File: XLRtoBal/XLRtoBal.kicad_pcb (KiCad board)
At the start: 2 copper layers, 85 x 93 mm, 55 parts, among them J1 XLR3, J10 Conn_Coaxial, J11 Conn_Coaxial, J2 Conn_01x04, J3 Conn_01x04, J4 XLR3, J5 Conn_01x04, J6 Conn_01x01, J7 Conn_01x01, J8 Conn_01x01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

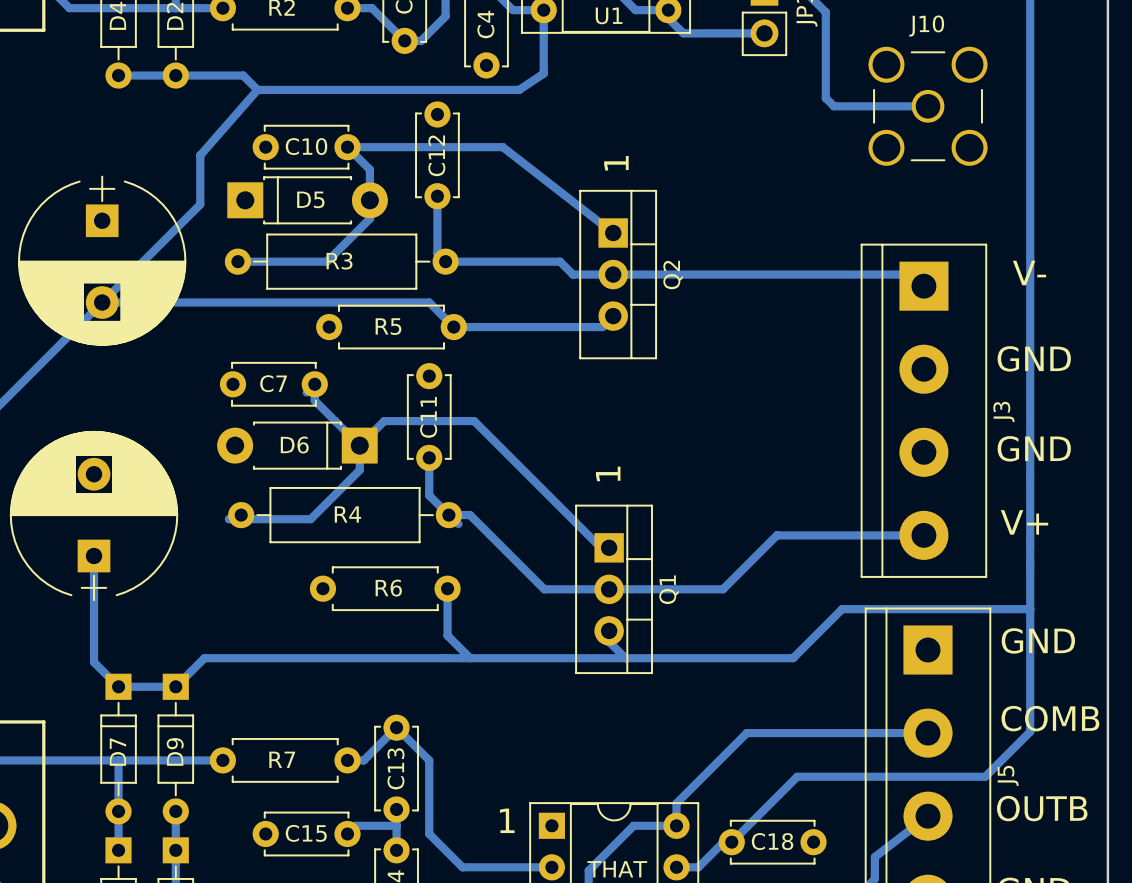
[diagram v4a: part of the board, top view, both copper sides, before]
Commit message: Changed to 2N5551/2N5401 from BC546C/BC556C transistors
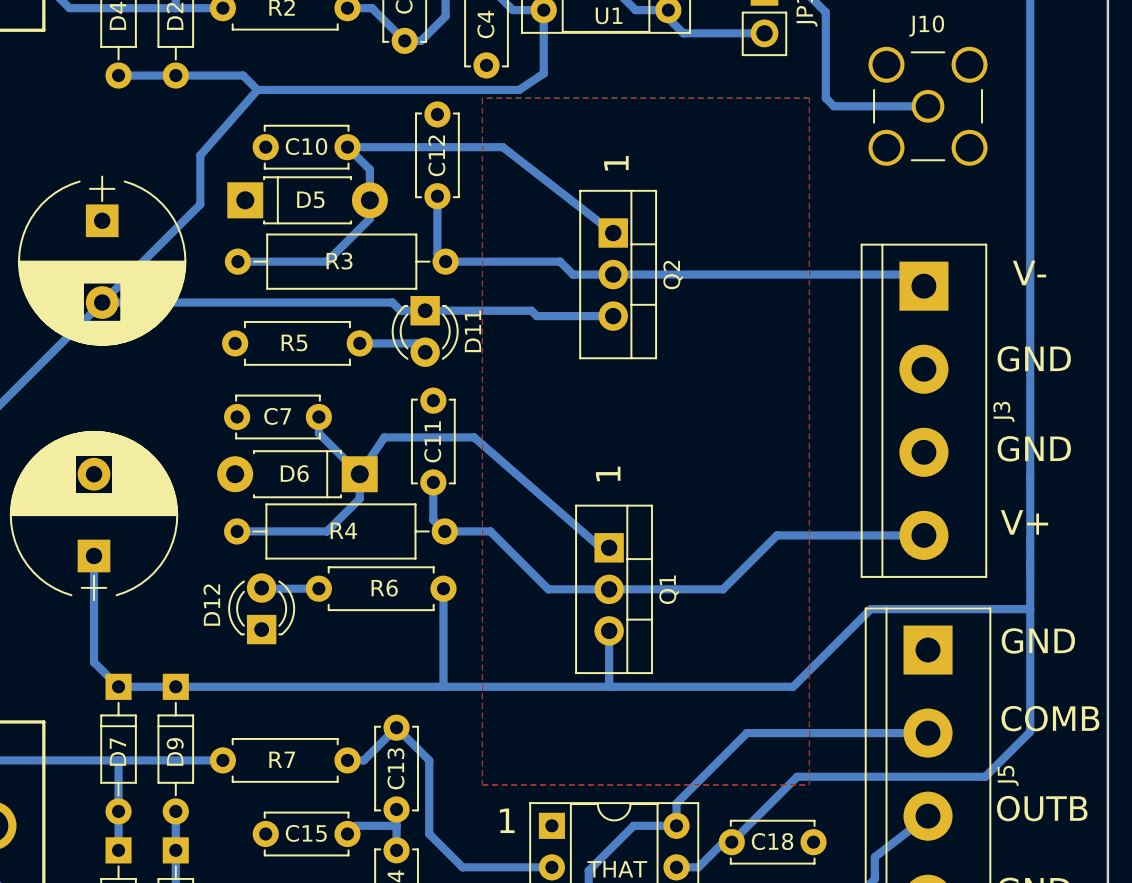
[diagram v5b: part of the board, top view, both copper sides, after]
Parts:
- added D11: LED, LEDs:LED_D3.0mm, F.Cu at (145.2, 101.5)
- added D12: LED, LEDs:LED_D3.0mm, F.Cu at (135.2, 121.0)
- J1, J4: value XLR3 -> XLR-04WP
- J10, J11: value Conn_Coaxial -> SMAPCB
- R3, R4: value 4k7 -> 6k8
- R5, R6: value 1k -> 2k2
- moved R5 5.84 mm to (141.2, 103.5)
- moved C7 2.02 mm to (133.8, 108.0)
- moved D6 1.75 mm to (141.2, 111.5)
- moved C11 1.52 mm to (145.8, 107.0)
- moved R4 1.03 mm to (133.8, 115.0)
- moved R6 0.25 mm to (138.8, 118.5)
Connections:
- R5 pad 1: VEE -> Net-(D11-Pad2)
- R6 pad 1: GND -> Net-(D12-Pad2)
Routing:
- net Net-(D11-Pad2): track 0.00 -> 4.22 mm
- net Net-(D12-Pad2): track 0.00 -> 3.52 mm
- net VCC: track 227.9 -> 230.8 mm
- net Net-(C7-Pad2): track 36.2 -> 33.6 mm
- net Net-(C11-Pad2): track 38.4 -> 36.8 mm
- net VEE: track 174.4 -> 173.9 mm

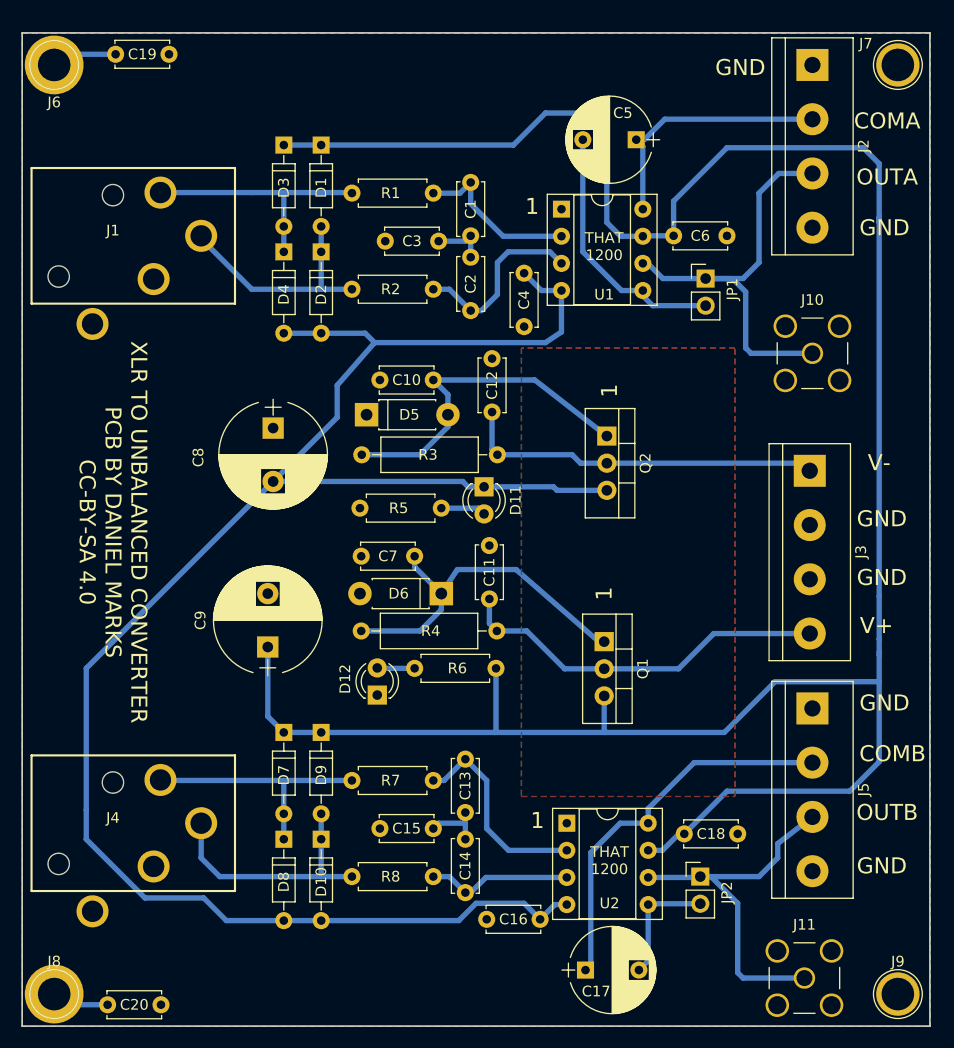
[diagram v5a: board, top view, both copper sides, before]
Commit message: Some more layout changed and XlrtoBal fix
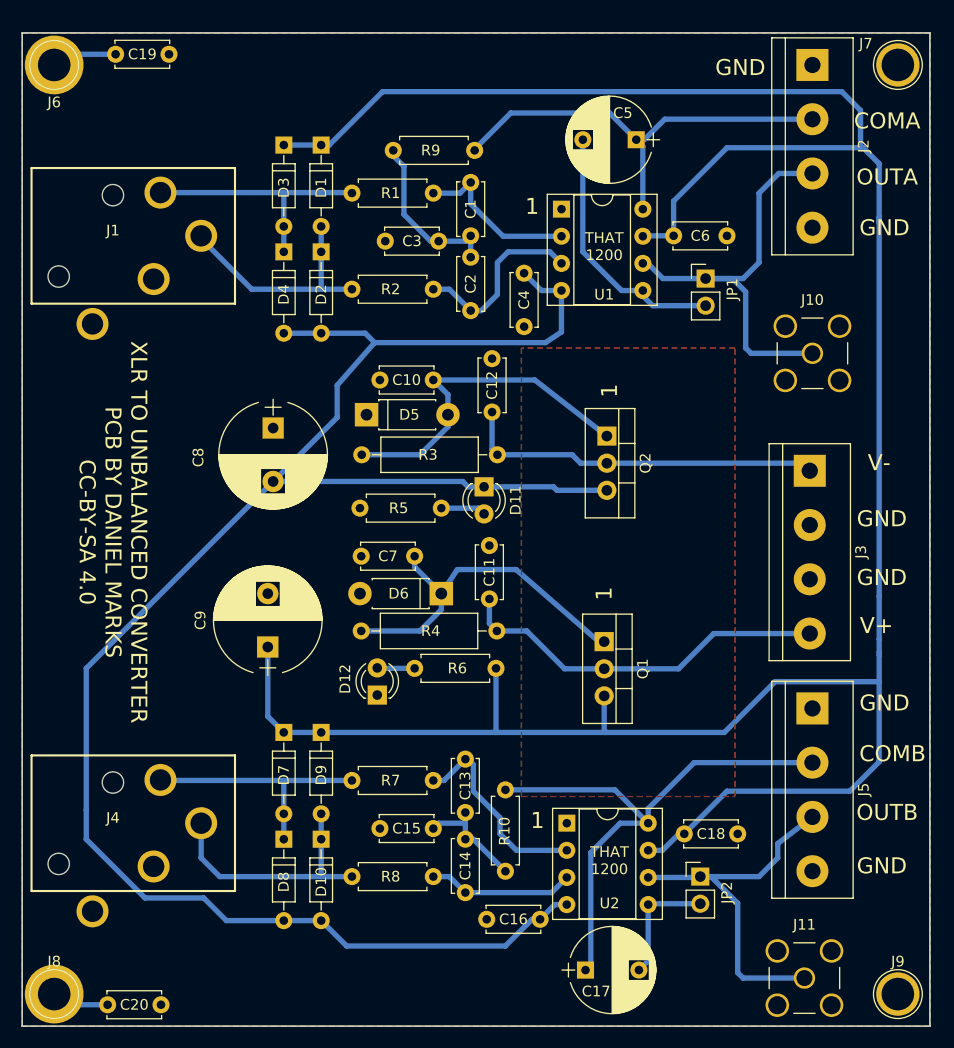
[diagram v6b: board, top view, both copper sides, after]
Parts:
- added R10: 4k7, Resistors_THT:R_Axial_DIN0207_L6.3mm_D2.5mm_P7.62mm_Horizontal, F.Cu at (147.2, 137.5)
- added R9: 4k7, Resistors_THT:R_Axial_DIN0207_L6.3mm_D2.5mm_P7.62mm_Horizontal, F.Cu at (136.8, 70.0)
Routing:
- net Net-(C5-Pad1): track 24.1 -> 41.7 mm
- net VCC: track 230.8 -> 246.1 mm
- net Net-(C17-Pad1): track 37.0 -> 51.7 mm
- net Net-(C1-Pad1): track 5.21 -> 15.9 mm
- net Net-(C13-Pad1): track 5.71 -> 10.9 mm
- net VEE: track 173.9 -> 174.6 mm
- net Net-(C14-Pad1): track 13.7 -> 14.2 mm

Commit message: Changed grounding and star layout
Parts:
- removed C19, C20: 100 nF, Capacitors_THT:C_Disc_D5.0mm_W2.5mm_P5.00mm
- added J12: Conn_01x02, Connectors_Terminal_Blocks:TerminalBlock_bornier-2_P5.08mm, F.Cu at (107.0, 103.9)
- added JP3: Jumper_NO_Small, Pin_Headers:Pin_Header_Straight_1x02_Pitch2.54mm, F.Cu at (113.8, 62.0)
- added JP4: Jumper_NO_Small, Pin_Headers:Pin_Header_Straight_1x02_Pitch2.54mm, F.Cu at (113.8, 148.6)
- J1, J4: value XLR-04WP -> XLR4BODYPIN
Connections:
- J1 pad G: (no net) -> GND
- J4 pad G: (no net) -> GND
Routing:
- net Net-(J6-Pad1): track 6.16 -> 7.69 mm
- net Net-(J8-Pad1): track 5.41 -> 6.45 mm

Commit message: Added option for spade terminal power connections
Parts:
- J12: footprint Connectors_Terminal_Blocks:TerminalBlock_bornier-2_P5.08mm -> XLRtoBal:TerminalBlock_bornier-2_P5.08mm_with_spade
- J3: footprint Connectors_Terminal_Blocks:TerminalBlock_bornier-4_P5.08mm -> XLRtoBal:TerminalBlock_bornier-4_P5.08mm_with_spade
- moved J3 3.50 mm to (172.2, 100.0)
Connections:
- J3 pad 1: Net-(C12-Pad1) -> GND
- J3 pad 2: GND -> Net-(C12-Pad1)
- J3 pad 3: GND -> Net-(C11-Pad2)
- J3 pad 4: Net-(C11-Pad2) -> GND
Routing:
- net GND: track 0.00 -> 3.11 mm
- net Net-(C11-Pad2): track 36.8 -> 39.5 mm
- net Net-(C12-Pad1): track 35.9 -> 38.5 mm
